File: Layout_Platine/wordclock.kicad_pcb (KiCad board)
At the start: 2 copper layers, 80 x 50.8 mm, 75 parts, among them IC1 ATMEGA, P1 DCF_CONN_4, P10 CONN_1, P101 CONN_01X03, P102 CONN_01X01, P13 P_led, P14 CONN_2, P2 5V_CONN_2, P3 ISP, P4 UART_CONN_6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

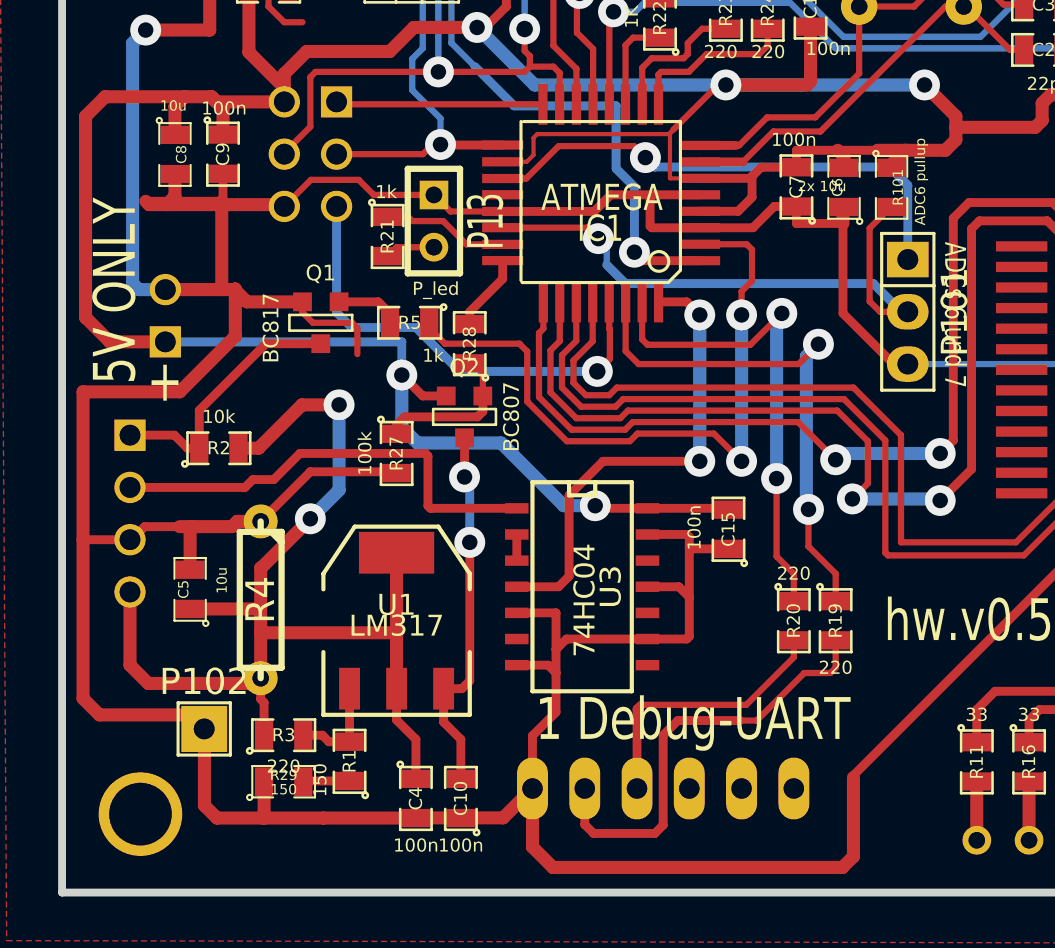
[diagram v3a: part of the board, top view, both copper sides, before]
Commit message: Testprogramm für die Minutenleds dazugefügt
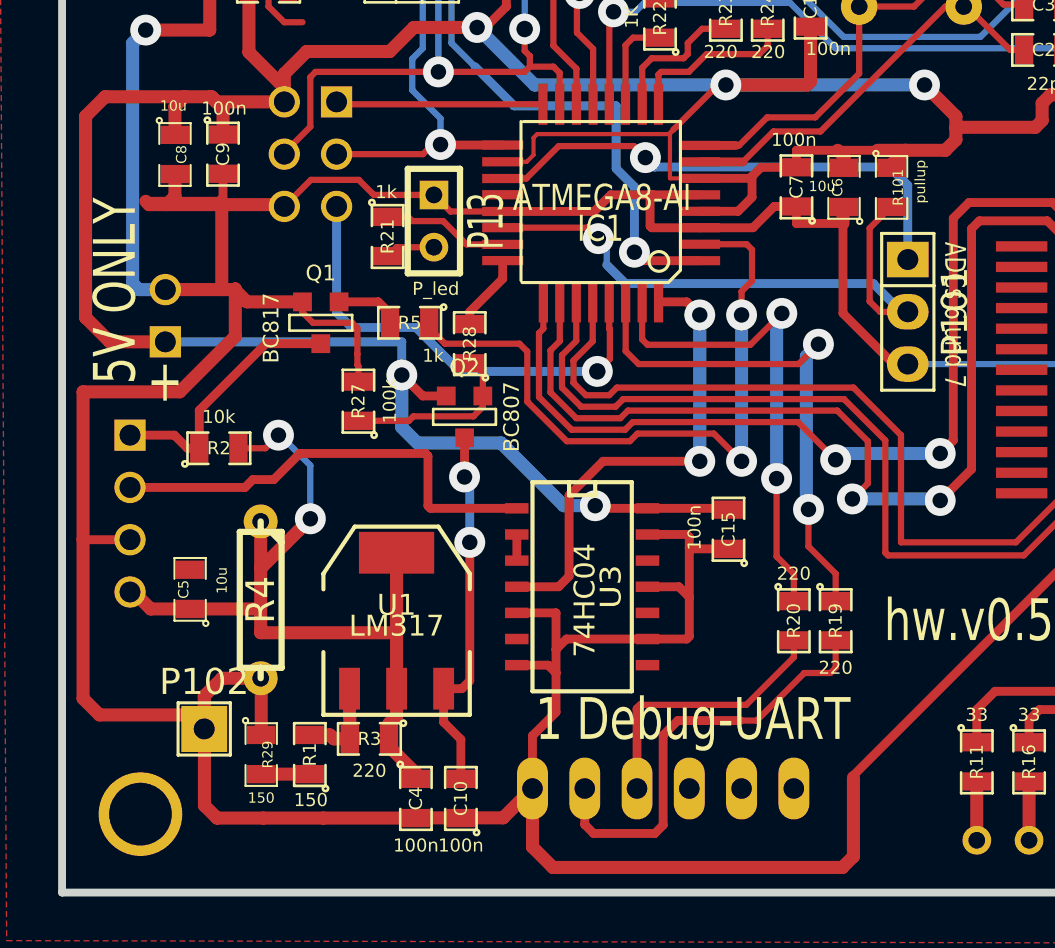
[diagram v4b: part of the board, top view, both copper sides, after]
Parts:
- C6: value 2x 10u -> 10u
- IC1: value ATMEGA -> ATMEGA8-AI
- R101: value ADC6 pullup -> pullup
- moved R3 4.17 mm to (185.1, 80.2), turned to 180 degrees
- moved R27 3.14 mm to (184.6, 63.8), turned to 90 degrees
- moved R1 1.96 mm to (182.2, 80.9)
- moved R29 1.71 mm to (179.9, 80.9), turned to 270 degrees
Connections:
- DS1 pad 1: Net-(DS1-Pad1) -> (no net)
- DS1 pad 4: Net-(DS1-Pad4) -> (no net)
- HT1 pad 1: Net-(HT1-Pad1) -> (no net)
- HT1 pad 15: Net-(HT1-Pad15) -> (no net)
- HT1 pad 20: Net-(HT1-Pad20) -> (no net)
- HT1 pad 34: Net-(HT1-Pad34) -> (no net)
- HT1 pad 35: Net-(HT1-Pad35) -> (no net)
- HT1 pad 37: Net-(HT1-Pad37) -> (no net)
- HT1 pad 39: Net-(HT1-Pad39) -> (no net)
- HT1 pad 40: Net-(HT1-Pad40) -> (no net)
- HT1 pad 41: Net-(HT1-Pad41) -> (no net)
- HT1 pad 42: Net-(HT1-Pad42) -> (no net)
- HT1 pad 43: Net-(HT1-Pad43) -> (no net)
- HT1 pad 44: Net-(HT1-Pad44) -> (no net)
- HT1 pad 45: Net-(HT1-Pad45) -> (no net)
- HT1 pad 46: Net-(HT1-Pad46) -> (no net)
- HT1 pad 47: Net-(HT1-Pad47) -> (no net)
- HT1 pad 48: Net-(HT1-Pad48) -> (no net)
- HT1 pad 49: Net-(HT1-Pad49) -> (no net)
- HT1 pad 50: Net-(HT1-Pad50) -> (no net)
- HT1 pad 51: Net-(HT1-Pad51) -> (no net)
- HT1 pad 52: Net-(HT1-Pad52) -> (no net)
- IC1 pad 20: Net-(C17-Pad1) -> (no net)
- P10 pad 1: Net-(P10-Pad1) -> (no net)
- P4 pad 4: Net-(P4-Pad4) -> (no net)
- P4 pad 5: Net-(P4-Pad5) -> (no net)
- P4 pad 6: Net-(P4-Pad6) -> (no net)
- P7 pad 1: Net-(P7-Pad1) -> (no net)
- P8 pad 1: Net-(P8-Pad1) -> (no net)
- P9 pad 1: Net-(P9-Pad1) -> (no net)
- U3 pad 10: Net-(U3-Pad10) -> (no net)
- U3 pad 12: Net-(U3-Pad12) -> (no net)
- U3 pad 6: Net-(U3-Pad6) -> (no net)
- U3 pad 8: Net-(U3-Pad8) -> (no net)
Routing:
- net /3V: track 56.0 -> 41.2 mm
- net GND: track 377.3 -> 368.4 mm
- net Net-(Q2-Pad2): track 7.62 -> 8.82 mm
